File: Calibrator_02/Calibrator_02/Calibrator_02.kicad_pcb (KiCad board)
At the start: 2 copper layers, 90 parts, among them J1 DB9_Female_MountingHoles, J2 Conn_01x01_Female, J3 Conn_01x01_Female, J4 Conn_01x04, J5 Conn_01x04, J6 Conn_Coaxial, U1 KAQY214STLD, U10 AW9523BTQR, U11 KAQY214STLD, U12 KAQY214STLD, U13 KAQY214STLD, U14 KAQY214STLD, U15 KAQY214STLD, U16 KAQY214STLD, U17 KAQY214STLD, U18 KAQY214STLD, U19 KAQY214STLD, U2 KAQY214STLD, U20 KAQY214STLD, U21 KAQY214STLD, U22 KAQY214STLD, U23 KAQY214STLD, U24 KAQY214STLD, U25 KAQY214STLD, U26 KAQY214STLD, U27 KAQY214STLD, U28 KAQY214STLD, U29 KAQY214STLD, U3 KAQY214STLD, U30 KAQY214STLD, U31 KAQY214STLD, U32 KAQY214STLD, U33 KAQY214STLD, U34 KAQY214STLD, U4 KAQY214STLD, U5 KAQY214STLD, U6 KAQY214STLD, U7 KAQY214STLD, U8 KAQY214STLD

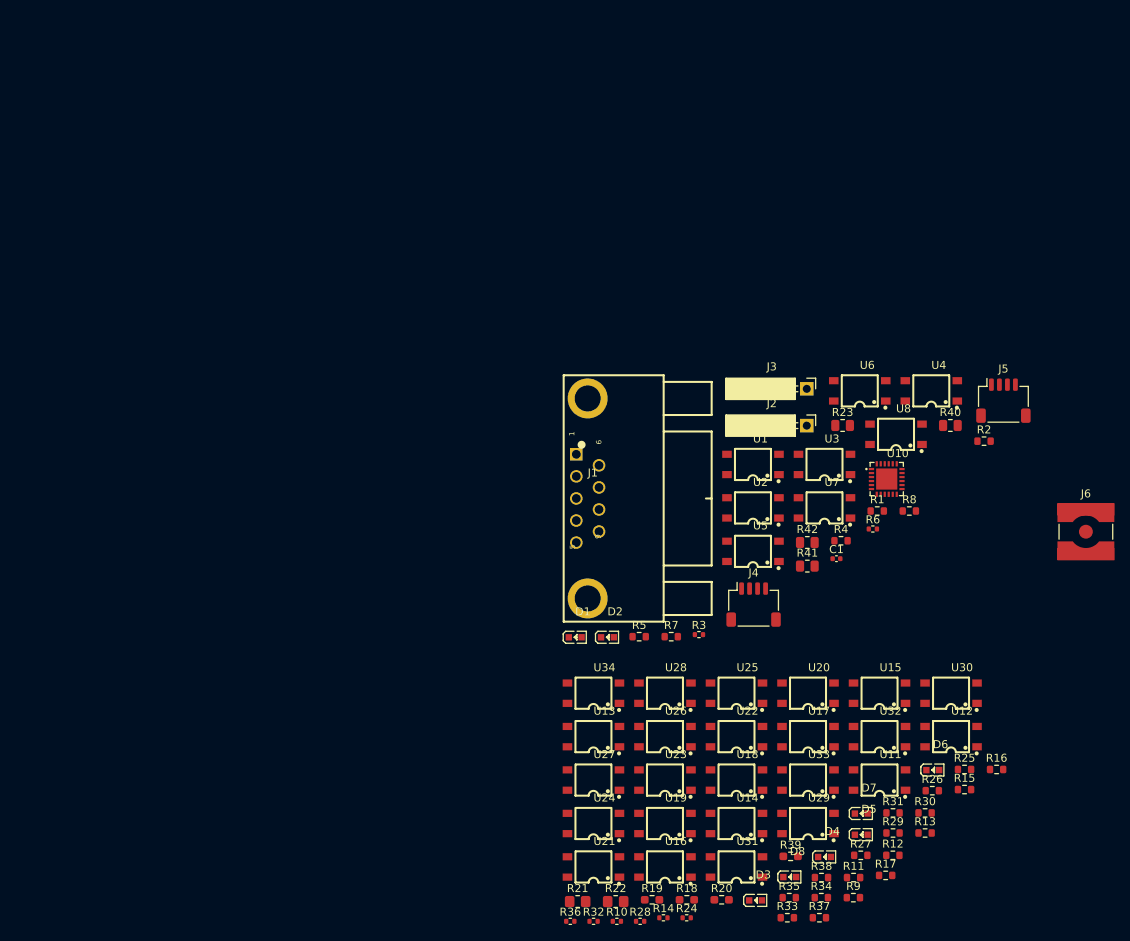
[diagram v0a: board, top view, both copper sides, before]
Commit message: Fixed jst pinouts and made Cali board
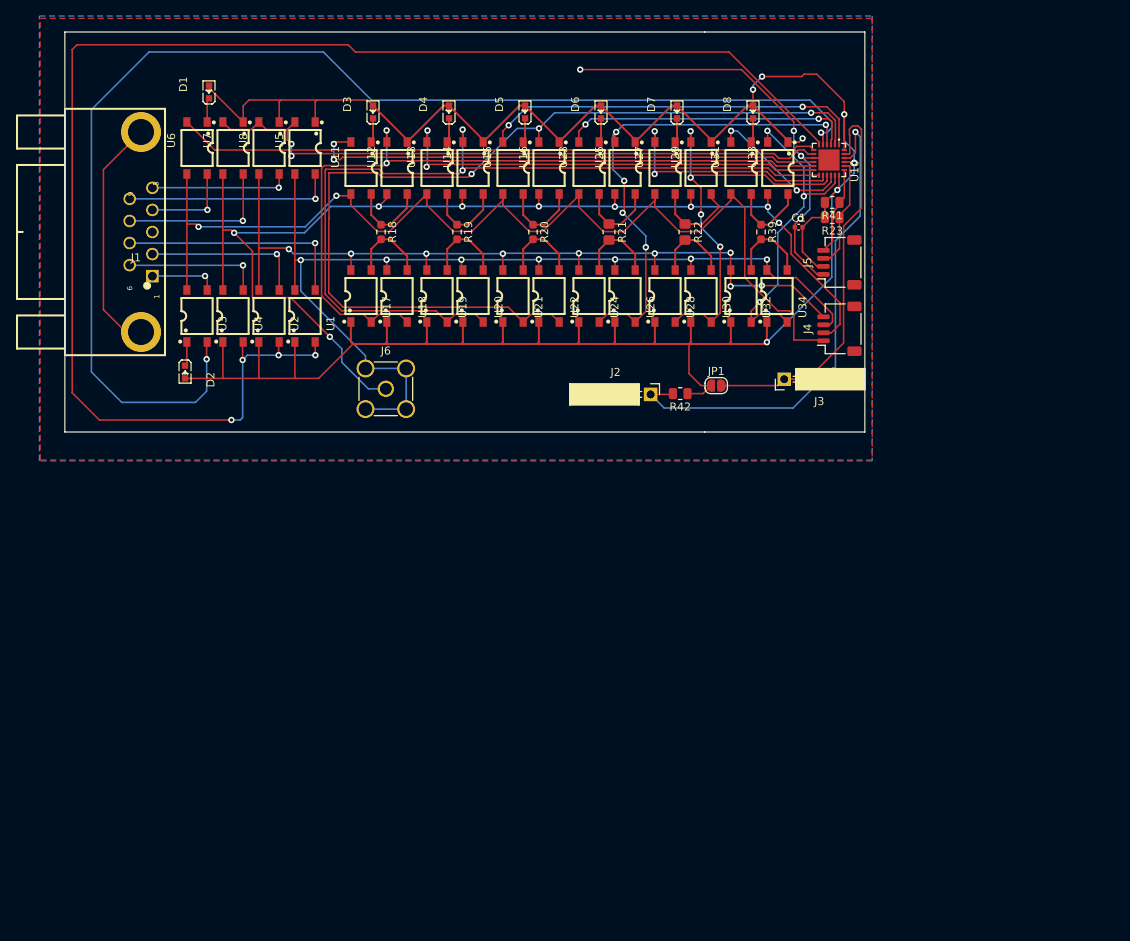
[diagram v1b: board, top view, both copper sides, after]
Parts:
- removed R1, R11, R12, R13, R15, R16, R17, R2, R25, R26, R27, R29, R30, R31, R33, R34, R35, R37, R38, R4, R5, R7, R8, R9: 390, Resistor_SMD:R_0603_1608Metric
- removed R10, R14, R24, R28, R3, R32, R36, R6: 240, Resistor_SMD:R_0402_1005Metric
- removed R40: 4.7K, Resistor_SMD:R_0805_2012Metric
- added JP1: Jumper, Jumper:SolderJumper-2_P1.3mm_Open_RoundedPad1.0x1.5mm, F.Cu at (71.9, 19.2)
- J6: footprint Connector_Coaxial:SMA_Amphenol_132134-10_Vertical -> Connector_Coaxial:SMA_Amphenol_901-144_Vertical
- moved D3 109.5 mm to (29.0, -15.0), turned to 90 degrees
- moved D4 104.3 mm to (38.5, -15.0), turned to 90 degrees
- moved U11 100.3 mm to (27.5, -8.00), turned to 90 degrees
- moved D5 99.6 mm to (48.0, -15.0), turned to 90 degrees
- moved U12 99.2 mm to (32.0, -8.00), turned to 90 degrees
- moved D8 95.7 mm to (76.5, -15.0), turned to 90 degrees
- moved D6 92.1 mm to (57.5, -15.0), turned to 90 degrees
- moved R18 91.8 mm to (30.0, 0.00), turned to 270 degrees
- moved D7 90.7 mm to (67.0, -15.0), turned to 90 degrees
- moved J6 89.3 mm to (30.6, 19.6)
- moved U16 88.6 mm to (51.0, -8.00), turned to 90 degrees
- moved U14 88.3 mm to (41.5, -8.00), turned to 90 degrees
- moved U6 88.2 mm to (7.00, -10.5), turned to 90 degrees
- moved U4 87.8 mm to (11.5, 10.5), turned to 270 degrees
- moved U31 87.4 mm to (75.0, -8.00), turned to 90 degrees
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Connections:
- D1 pad 2: Net-(D1-Pad2) -> +3V3
- D2 pad 2: Net-(D2-Pad2) -> +3V3
- D3 pad 2: Net-(D3-Pad2) -> +3V3
- D4 pad 2: Net-(D4-Pad2) -> +3V3
- D5 pad 2: Net-(D5-Pad2) -> +3V3
- D6 pad 2: Net-(D6-Pad2) -> +3V3
- D7 pad 2: Net-(D7-Pad2) -> +3V3
- D8 pad 2: Net-(D8-Pad2) -> +3V3
- J1 pad 3: GNDS -> GND
- J4 pad 3: /Resistor_Network/I- -> /Resistor_Network/V-
- J4 pad 4: /Resistor_Network/V- -> /Resistor_Network/I-
- J6 pad 1: Net-(J6-Pad1) -> /Resistor_Network/V+
- J6 pad 2: Net-(J6-Pad2) -> /Resistor_Network/V-
- R18 pad 1: Net-(J6-Pad1) -> Net-(R18-Pad1)
- R18 pad 2: Net-(J6-Pad2) -> Net-(R18-Pad2)
- U1 pad 1: Net-(R1-Pad2) -> +3V3
- U11 pad 4: Net-(J6-Pad1) -> Net-(R18-Pad1)
- U12 pad 1: Net-(R12-Pad2) -> +3V3
- U12 pad 4: Net-(J6-Pad1) -> Net-(R18-Pad1)
- U14 pad 1: Net-(R16-Pad2) -> +3V3
- U16 pad 1: Net-(R26-Pad2) -> +3V3
- U17 pad 1: Net-(R9-Pad1) -> +3V3
- U17 pad 3: Net-(J6-Pad2) -> Net-(R18-Pad2)
- U18 pad 1: Net-(R11-Pad1) -> +3V3
- U18 pad 3: Net-(J6-Pad2) -> Net-(R18-Pad2)
- U19 pad 1: Net-(R13-Pad1) -> +3V3
- U2 pad 1: Net-(R2-Pad2) -> +3V3
- U20 pad 1: Net-(R15-Pad1) -> +3V3
- U21 pad 1: Net-(R17-Pad1) -> +3V3
- U22 pad 1: Net-(R25-Pad1) -> +3V3
- U24 pad 1: Net-(R27-Pad1) -> +3V3
- U25 pad 1: Net-(R30-Pad2) -> +3V3
- U26 pad 1: Net-(R29-Pad1) -> +3V3
- U28 pad 1: Net-(R31-Pad1) -> +3V3
- U29 pad 1: Net-(R34-Pad2) -> +3V3
- U30 pad 1: Net-(R33-Pad1) -> +3V3
- U32 pad 1: Net-(R35-Pad1) -> +3V3
- U33 pad 1: Net-(R38-Pad2) -> +3V3
- U34 pad 1: Net-(R37-Pad1) -> +3V3
- U4 pad 1: Net-(R4-Pad2) -> +3V3
- U5 pad 1: Net-(R5-Pad1) -> +3V3
- U7 pad 1: Net-(R7-Pad1) -> +3V3
- U8 pad 1: Net-(R8-Pad1) -> +3V3
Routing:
- net +3V3: track 0.00 -> 315.9 mm, vias 0 -> 7
- net /I_01: track 0.00 -> 187.0 mm, vias 0 -> 4
- net /I_00: track 0.00 -> 158.6 mm, vias 0 -> 2
- net /Resistor_Network/V+: track 0.00 -> 146.4 mm, vias 0 -> 9
- net /Resistor_Network/I+: track 0.00 -> 135.7 mm, vias 0 -> 2
- net /Resistor_Network/V-: track 0.00 -> 126.6 mm, vias 0 -> 7
- net /I_11: track 0.00 -> 118.1 mm, vias 0 -> 3
- net /I_07: track 0.00 -> 106.9 mm, vias 0 -> 2
- net /Resistor_Network/I-: track 0.00 -> 101.6 mm, vias 0 -> 9
- net /I_05: track 0.00 -> 96.5 mm, vias 0 -> 2
- net /I_03: track 0.00 -> 80.4 mm, vias 0 -> 2
- net /I_02: track 0.00 -> 80.2 mm
- net /I_04: track 0.00 -> 64.5 mm, vias 0 -> 2
- net Net-(J2-Pad1): track 0.00 -> 64.0 mm, vias 0 -> 1
- net /I_13: track 0.00 -> 62.1 mm, vias 0 -> 5
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- added copper zone on B.Cu, net GND
- added copper zone on F.Cu, net GND
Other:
- board outline added: 100 x 50 mm
- net class Default: clearance 0.2 -> 0.25; trace_width 0.25 -> 0.2
- rule trace_clearance: 0.2 -> 0.25

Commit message: Update
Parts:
- moved J5 16.8 mm to (80.4, 22.1), turned to 180 degrees
- moved R1 9.51 mm to (76.7, 22.2), turned to 0 degrees
- renumbered D2 to D1, D1 to D2, J4 to J1, J1 to J2, J6 to J3, J3 to J4, J2 to J5, J5 to J6, U10 to M1, R42 to R1, R41 to R2, R23 to R3, R19 to R4, R20 to R5, R21 to R6, R22 to R7, R18 to R8, R39 to R9, U12 to U10, U13 to U11, U14 to U12, U15 to U13, U16 to U14, U23 to U15, U25 to U16, U27 to U17, U29 to U18, U31 to U19, U33 to U20, U17 to U21, U18 to U22, U19 to U23, U20 to U24, U21 to U25, U22 to U26, U24 to U27, U26 to U28, U28 to U29, U32 to U31, U34 to U32, U11 to U9
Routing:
- net Net-(J5-Pad1): track 64.0 -> 46.6 mm
- net +3V3: track 315.9 -> 320.5 mm
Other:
- board text added: "Calibrator_02 Ryan Morgenstern 5/16/2022"

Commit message: update
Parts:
- moved C1 9.90 mm to (89.2, -7.60), turned to 90 degrees
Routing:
- net GND: track 55.7 -> 66.1 mm, vias 4 -> 5
- net +3V3: track 320.5 -> 322.1 mm

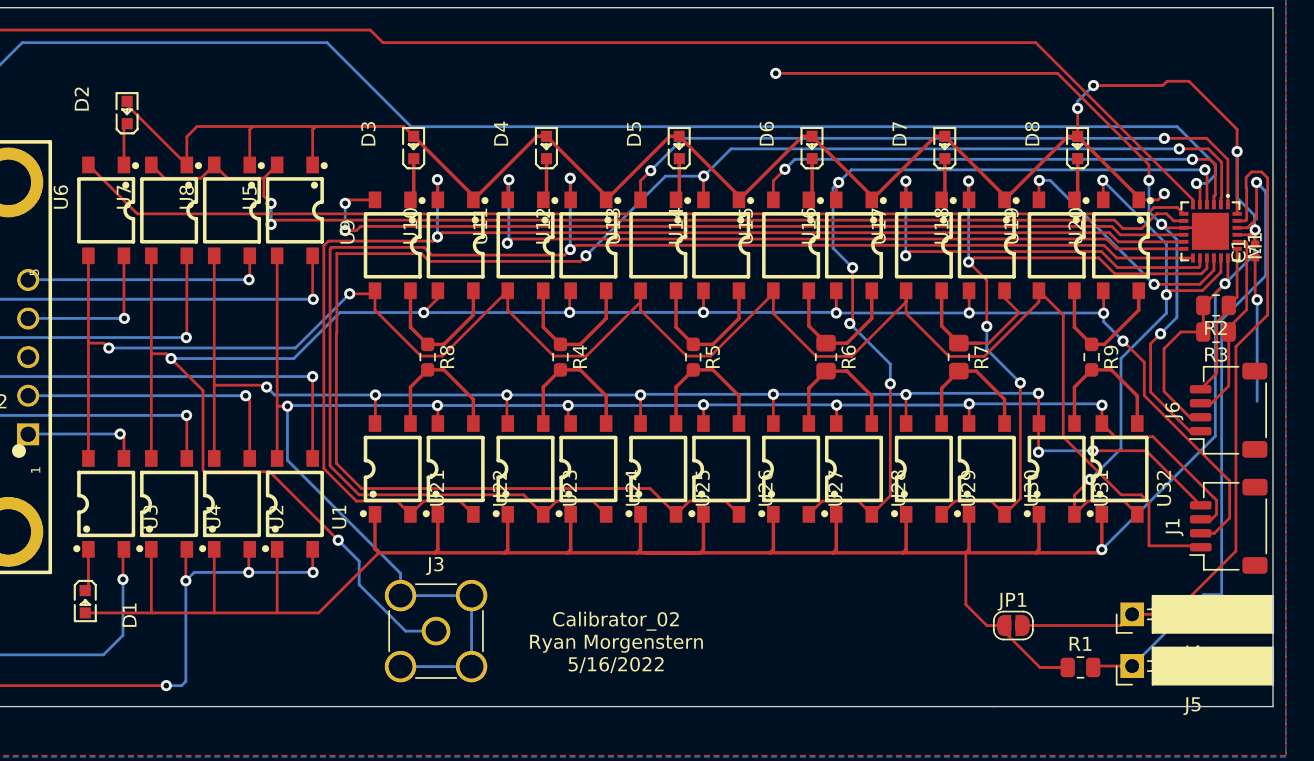
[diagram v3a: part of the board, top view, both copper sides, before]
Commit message: Added Resistors to Diodes
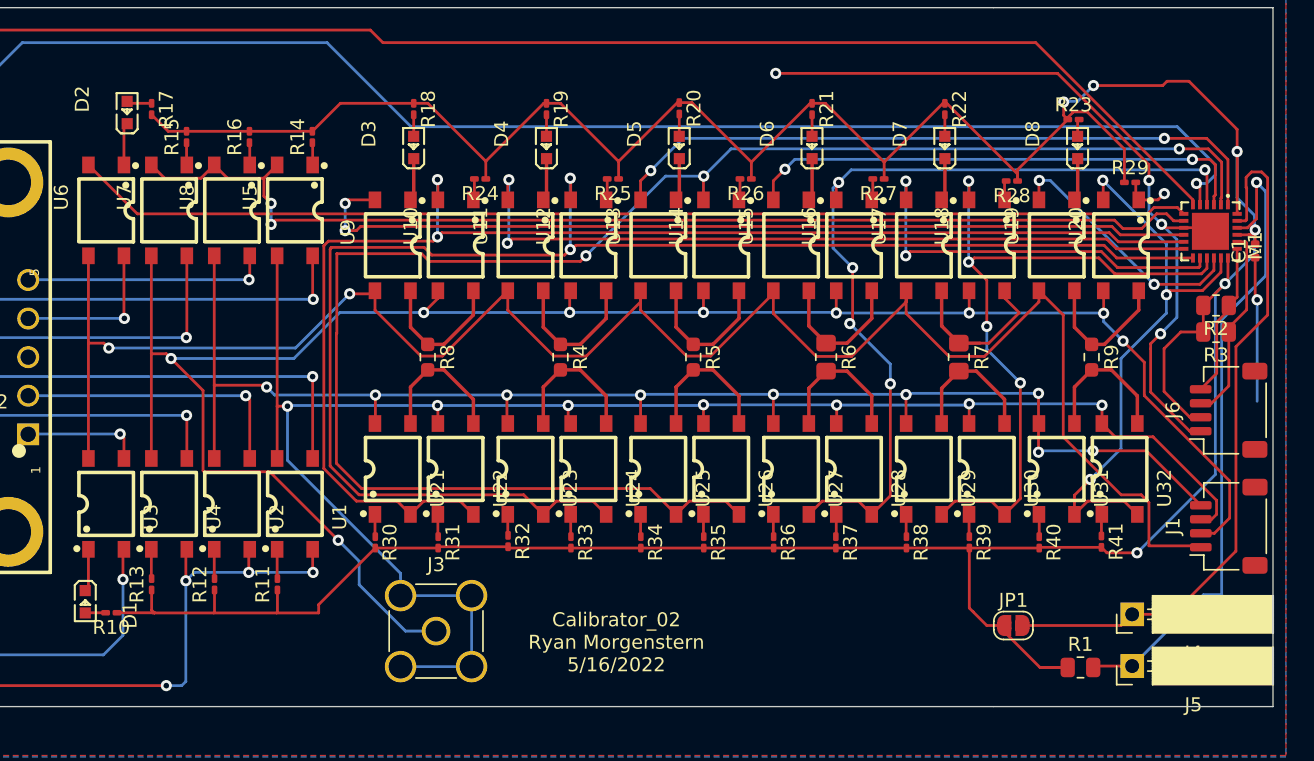
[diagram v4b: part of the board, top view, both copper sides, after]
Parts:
- added R10: 95.3 1%, Resistor_SMD:R_0201_0603Metric_Pad0.64x0.40mm_HandSolder, F.Cu at (7.37, 18.3)
- added R11: 84.5 1%, Resistor_SMD:R_0201_0603Metric_Pad0.64x0.40mm_HandSolder, F.Cu at (19.2, 16.2)
- added R12: 84.5 1%, Resistor_SMD:R_0201_0603Metric_Pad0.64x0.40mm_HandSolder, F.Cu at (14.8, 16.2)
- added R13: 84.5 1%, Resistor_SMD:R_0201_0603Metric_Pad0.64x0.40mm_HandSolder, F.Cu at (10.2, 16.2)
- added R14: 84.5 1%, Resistor_SMD:R_0201_0603Metric_Pad0.64x0.40mm_HandSolder, F.Cu at (21.8, -15.8)
- added R15: 84.5 1%, Resistor_SMD:R_0201_0603Metric_Pad0.64x0.40mm_HandSolder, F.Cu at (12.8, -15.8)
- added R16: 84.5 1%, Resistor_SMD:R_0201_0603Metric_Pad0.64x0.40mm_HandSolder, F.Cu at (17.2, -15.8)
- added R17: 95.3 1%, Resistor_SMD:R_0201_0603Metric_Pad0.64x0.40mm_HandSolder, F.Cu at (10.2, -17.8)
- added R18: 95.3 1%, Resistor_SMD:R_0201_0603Metric_Pad0.64x0.40mm_HandSolder, F.Cu at (29.0, -17.8)
- added R19: 95.3 1%, Resistor_SMD:R_0201_0603Metric_Pad0.64x0.40mm_HandSolder, F.Cu at (38.5, -17.8)
- added R20: 95.3 1%, Resistor_SMD:R_0201_0603Metric_Pad0.64x0.40mm_HandSolder, F.Cu at (48.0, -17.8)
- added R21: 95.3 1%, Resistor_SMD:R_0201_0603Metric_Pad0.64x0.40mm_HandSolder, F.Cu at (57.5, -17.8)
- added R22: 95.3 1%, Resistor_SMD:R_0201_0603Metric_Pad0.64x0.40mm_HandSolder, F.Cu at (67.0, -17.8)
- added R23: 95.3 1%, Resistor_SMD:R_0201_0603Metric_Pad0.64x0.40mm_HandSolder, F.Cu at (76.2, -17.0)
- added R24: 84.5 1%, Resistor_SMD:R_0201_0603Metric_Pad0.64x0.40mm_HandSolder, F.Cu at (33.8, -12.8)
- added R25: 84.5 1%, Resistor_SMD:R_0201_0603Metric_Pad0.64x0.40mm_HandSolder, F.Cu at (43.2, -12.8)
- added R26: 84.5 1%, Resistor_SMD:R_0201_0603Metric_Pad0.64x0.40mm_HandSolder, F.Cu at (52.8, -12.8)
- added R27: 84.5 1%, Resistor_SMD:R_0201_0603Metric_Pad0.64x0.40mm_HandSolder, F.Cu at (62.2, -12.8)
- added R28: 84.5 1%, Resistor_SMD:R_0201_0603Metric_Pad0.64x0.40mm_HandSolder, F.Cu at (71.8, -12.6)
- added R29: 84.5 1%, Resistor_SMD:R_0201_0603Metric_Pad0.64x0.40mm_HandSolder, F.Cu at (80.2, -12.5)
- added R30: 84.5 1%, Resistor_SMD:R_0201_0603Metric_Pad0.64x0.40mm_HandSolder, F.Cu at (26.2, 13.2)
- added R31: 84.5 1%, Resistor_SMD:R_0201_0603Metric_Pad0.64x0.40mm_HandSolder, F.Cu at (30.8, 13.2)
- added R32: 84.5 1%, Resistor_SMD:R_0201_0603Metric_Pad0.64x0.40mm_HandSolder, F.Cu at (35.8, 13.2)
- added R33: 84.5 1%, Resistor_SMD:R_0201_0603Metric_Pad0.64x0.40mm_HandSolder, F.Cu at (40.2, 13.2)
- added R34: 84.5 1%, Resistor_SMD:R_0201_0603Metric_Pad0.64x0.40mm_HandSolder, F.Cu at (45.2, 13.2)
- added R35: 84.5 1%, Resistor_SMD:R_0201_0603Metric_Pad0.64x0.40mm_HandSolder, F.Cu at (49.8, 13.2)
- added R36: 84.5 1%, Resistor_SMD:R_0201_0603Metric_Pad0.64x0.40mm_HandSolder, F.Cu at (54.8, 13.2)
- added R37: 84.5 1%, Resistor_SMD:R_0201_0603Metric_Pad0.64x0.40mm_HandSolder, F.Cu at (59.2, 13.2)
- added R38: 84.5 1%, Resistor_SMD:R_0201_0603Metric_Pad0.64x0.40mm_HandSolder, F.Cu at (64.2, 13.2)
- added R39: 84.5 1%, Resistor_SMD:R_0201_0603Metric_Pad0.64x0.40mm_HandSolder, F.Cu at (68.8, 13.2)
- added R40: 84.5 1%, Resistor_SMD:R_0201_0603Metric_Pad0.64x0.40mm_HandSolder, F.Cu at (73.8, 13.2)
- added R41: 84.5 1%, Resistor_SMD:R_0201_0603Metric_Pad0.64x0.40mm_HandSolder, F.Cu at (78.2, 13.2)
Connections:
- D1 pad 2: +3V3 -> Net-(D1-Pad2)
- D2 pad 2: +3V3 -> Net-(D2-Pad2)
- D3 pad 2: +3V3 -> Net-(D3-Pad2)
- D4 pad 2: +3V3 -> Net-(D4-Pad2)
- D5 pad 2: +3V3 -> Net-(D5-Pad2)
- D6 pad 2: +3V3 -> Net-(D6-Pad2)
- D7 pad 2: +3V3 -> Net-(D7-Pad2)
- D8 pad 2: +3V3 -> Net-(D8-Pad2)
- U1 pad 1: +3V3 -> Net-(R11-Pad2)
- U10 pad 1: +3V3 -> Net-(R24-Pad2)
- U12 pad 1: +3V3 -> Net-(R25-Pad2)
- U14 pad 1: +3V3 -> Net-(R26-Pad2)
- U16 pad 1: +3V3 -> Net-(R27-Pad2)
- U18 pad 1: +3V3 -> Net-(R28-Pad2)
- U2 pad 1: +3V3 -> Net-(R12-Pad2)
- U20 pad 1: +3V3 -> Net-(R29-Pad2)
- U21 pad 1: +3V3 -> Net-(R30-Pad1)
- U22 pad 1: +3V3 -> Net-(R31-Pad1)
- U23 pad 1: +3V3 -> Net-(R32-Pad1)
- U24 pad 1: +3V3 -> Net-(R33-Pad1)
- U25 pad 1: +3V3 -> Net-(R34-Pad1)
- U26 pad 1: +3V3 -> Net-(R35-Pad1)
- U27 pad 1: +3V3 -> Net-(R36-Pad1)
- U28 pad 1: +3V3 -> Net-(R37-Pad1)
- U29 pad 1: +3V3 -> Net-(R38-Pad1)
- U30 pad 1: +3V3 -> Net-(R39-Pad1)
- U31 pad 1: +3V3 -> Net-(R40-Pad1)
- U32 pad 1: +3V3 -> Net-(R41-Pad1)
- U4 pad 1: +3V3 -> Net-(R13-Pad2)
- U5 pad 1: +3V3 -> Net-(R14-Pad1)
- U7 pad 1: +3V3 -> Net-(R15-Pad1)
- U8 pad 1: +3V3 -> Net-(R16-Pad1)
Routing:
- net +3V3: track 322.1 -> 267.8 mm, vias 7 -> 6
- net Net-(R29-Pad2): track 0.00 -> 3.84 mm, vias 0 -> 1
- net Net-(R13-Pad2): track 0.00 -> 2.10 mm
- net Net-(R12-Pad2): track 0.00 -> 2.10 mm
- net Net-(R11-Pad2): track 0.00 -> 2.10 mm
- net Net-(D2-Pad2): track 0.00 -> 2.09 mm
- net Net-(R28-Pad2): track 0.00 -> 1.84 mm
- net Net-(R27-Pad2): track 0.00 -> 1.81 mm
- net Net-(R26-Pad2): track 0.00 -> 1.81 mm
- net Net-(R25-Pad2): track 0.00 -> 1.81 mm
- net Net-(R24-Pad2): track 0.00 -> 1.81 mm
- net Net-(R37-Pad1): track 0.00 -> 1.60 mm
- net Net-(R36-Pad1): track 0.00 -> 1.60 mm
- net Net-(R35-Pad1): track 0.00 -> 1.60 mm
- net Net-(R34-Pad1): track 0.00 -> 1.60 mm
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
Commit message: Update
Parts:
- removed JP1: Jumper, Jumper:SolderJumper-2_P1.3mm_Open_RoundedPad1.0x1.5mm
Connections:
- J4 pad 1: Net-(J4-Pad1) -> +3V3
- M1 pad 23: Net-(J4-Pad1) -> +3V3
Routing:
- net +3V3: track 267.8 -> 324.6 mm, vias 6 -> 7
- net Net-(J4-Pad1): track 50.8 -> 0.00 mm

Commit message: Update
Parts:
- removed J4: Conn_01x01_Female, Connector_PinSocket_2.54mm:PinSocket_1x01_P2.54mm_Horizontal
- moved J5 1.60 mm to (80.5, 20.5)
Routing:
- net Net-(J5-Pad1): track 46.7 -> 47.3 mm
